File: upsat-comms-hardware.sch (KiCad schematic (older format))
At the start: 195 parts, among them J1 SMA, J2 SMA, P1 SWD, P2 OBC, P3 CONN_02X03, U1 TXCO_TG_5021CG, U10 CC1120, U12 ADT7420, U14 OPA320, U16 RF5110G, U18 FA_128_, U2 TPS79930, U3 FA_128_, U4 CC1120, U5 STM32F407VG, U6 TXCO_TG_5021CG, U8 TPS79930, Y1 Crystal, Y2 Crystal

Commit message: Cleanup of zones and vias.
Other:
- note added: "TX"
- note removed: "CHECK DISCO GERBER"
- note removed: "EDW ISWS LATHOS \nSTON KOMVO PREPEI\nNA NAI APO PANW?"
- note removed: "MPORW NA THN PARALEIPSW THN 0\n"
- note removed: "MY OBC RX IS THE ACTUALL OBC TX"
- note removed: "Na dw ti ginetai me ta ground klp"
- note removed: "Na dw ti ginetai me ta ground klp kai toy stm gia ton DAC"
- note removed: "TX1"
- note removed: "WILL I PUT THE 0 OHM RES?\n"
- note removed: "distributed connections between RF and digital ground\nTODO check analog ground"
- moved on the sheet: RFSHIELD1
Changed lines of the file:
@@
 LIBS:F4
 LIBS:F4-cache
-LIBS:ADT7420
-LIBS:cc1120
-LIBS:dart-4460
-LIBS:hrs-dm3
-LIBS:tc74
 LIBS:sma
 LIBS:rf5110g
-LIBS:FA-128 32.0000MF20X-K3
-LIBS:fa128
 LIBS:txco_tg_5021cg
 LIBS:opa320
 LIBS:PE4259
 LIBS:TPS79930
-LIBS:FA_128
-LIBS:fa_128_
+LIBS:hrs-dm3
 LIBS:FA_128_
-LIBS:comms-hardware-diploma-theodoridis-cache
 EELAYER 25 0
 EELAYER END
@@
 	1    0    0    -1
 $EndComp
-Text Notes 2100 22750 0    60   ~ 0
-distributed connections between RF and digital ground\nTODO check analog ground
-Text Notes 6150 21900 0    197  ~ 0
-Na dw ti ginetai me ta ground klp
-Text Notes 1100 9900 0    197  ~ 0
-Na dw ti ginetai me ta ground klp kai toy stm gia ton DAC
 Text Notes 1600 18350 0    60   ~ 0
 L1 is a Bead to be mounted if the regulator U2 is not mounted,\nCC1120 ref des will default not use regulator\nCC1120/CC1125: do not mount: U2, C12, C41, C53\nTG5021CG is optional: do not mount L1 if regulator is mounted\n
@@
 	1    0    0    -1
 $EndComp
-Text Notes 2900 2200 0    60   ~ 0
-CHECK DISCO GERBER
 $Comp
 L INDUCTOR L11
@@
 Text Label 12100 3600 0    60   ~ 0
 2GPIO3
-Text Notes 19700 22250 0    60   ~ 0
-MY OBC RX IS THE ACTUALL OBC TX
 Text Notes 28500 2250 0    394  ~ 0
-TX1
+TX
 Text Notes 7900 12350 0    394  ~ 0
 RX
@@
 Text Label 2100 7600 2    60   ~ 0
 USART3_RX
-Text Notes 12600 9300 0    60   ~ 0
-WILL I PUT THE 0 OHM RES?\n
-Text Notes 1250 3000 2    60   ~ 0
-WILL I PUT THE 0 OHM RES?\n
 Text Label 20500 2100 2    60   ~ 0
 I2C1_SCL
@@
 Wire Wire Line
 	3050 17300 2500 17300
-Text Notes 26900 3250 0    60   ~ 0
-EDW ISWS LATHOS \nSTON KOMVO PREPEI\nNA NAI APO PANW?
-Text Notes 7450 9300 0    60   ~ 0
-MPORW NA THN PARALEIPSW THN 0\n
-Text Notes 1800 3450 0    60   ~ 0
-MPORW NA THN PARALEIPSW THN 0\n
 $Comp
 L GND #PWR0129
@@
 L TEST_1P RFSHIELD1
 U 1 1 57080FD5
-P 29350 17650
-F 0 "RFSHIELD1" H 29350 17920 50  0000 C CNN
-F 1 "TEST_1P" H 29350 17850 50  0000 C CNN
-F 2 "libs:BMI-S-x06" H 29550 17650 50  0000 C CNN
-F 3 "" H 29550 17650 50  0000 C CNN
-	1    29350 17650
+P 25150 9500
+F 0 "RFSHIELD1" H 25150 9770 50  0000 C CNN
+F 1 "TEST_1P" H 25150 9700 50  0000 C CNN
+F 2 "libs:BMI-S-x06" H 25350 9500 50  0000 C CNN
+F 3 "" H 25350 9500 50  0000 C CNN
+	1    25150 9500
 	1    0    0    -1
 $EndComp
 Wire Wire Line
-	29350 17650 29350 17900
+	25150 9500 25150 9750
 $Comp
 L GND #PWR0145
 U 1 1 5708250E
-P 29350 17900
-F 0 "#PWR0145" H 29350 17650 50  0001 C CNN
-F 1 "GND" H 29350 17750 50  0000 C CNN
-F 2 "" H 29350 17900 50  0000 C CNN
-F 3 "" H 29350 17900 50  0000 C CNN
-	1    29350 17900
+P 25150 9750
+F 0 "#PWR0145" H 25150 9500 50  0001 C CNN
+F 1 "GND" H 25150 9600 50  0000 C CNN
+F 2 "" H 25150 9750 50  0000 C CNN
+F 3 "" H 25150 9750 50  0000 C CNN
+	1    25150 9750
 	1    0    0    -1
 $EndComp

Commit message: Restructuring libraries.
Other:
- moved on the sheet: C21, C23, C27, C61, C7, C89, C96

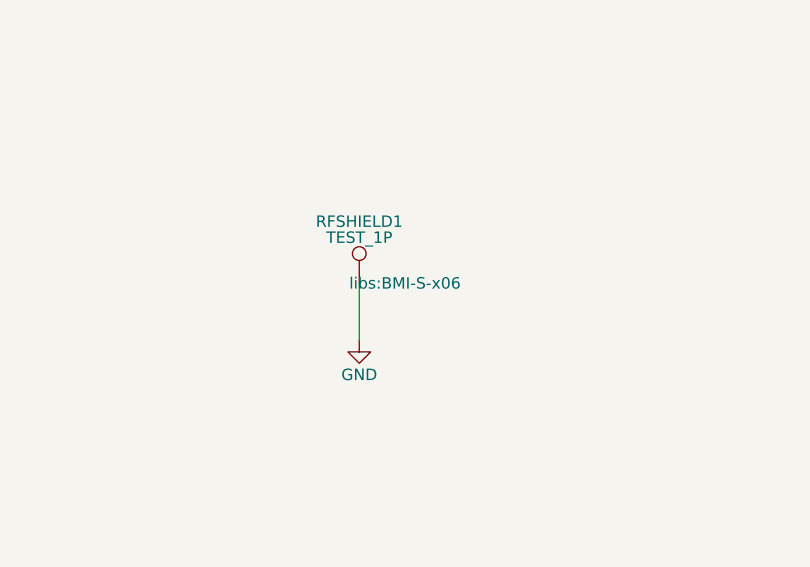
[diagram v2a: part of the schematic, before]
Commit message: Create silkscreen and reroute OBC Connector.
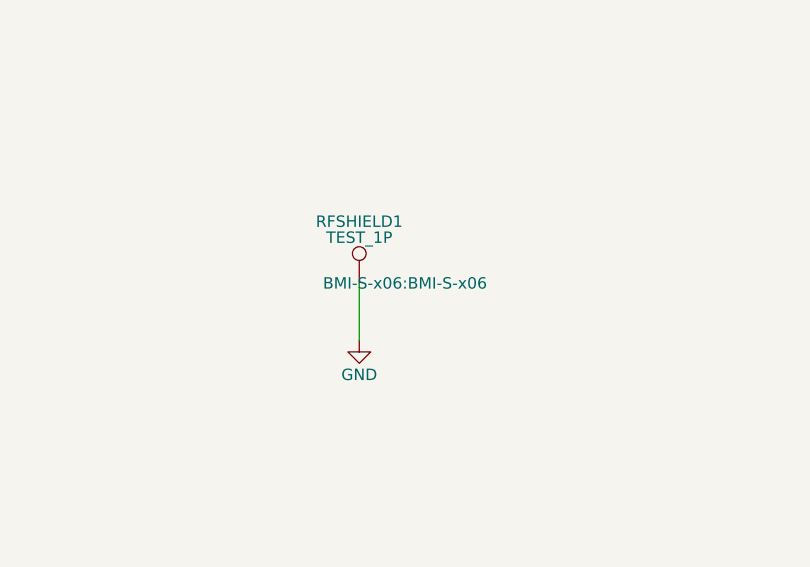
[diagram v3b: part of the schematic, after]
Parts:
- RFSHIELD1: footprint libs:BMI-S-x06 -> BMI-S-x06:BMI-S-x06
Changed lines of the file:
@@
 F 0 "RFSHIELD1" H 25150 9770 50  0000 C CNN
 F 1 "TEST_1P" H 25150 9700 50  0000 C CNN
-F 2 "libs:BMI-S-x06" H 25350 9500 50  0000 C CNN
+F 2 "BMI-S-x06:BMI-S-x06" H 25350 9500 50  0000 C CNN
 F 3 "" H 25350 9500 50  0000 C CNN
 	1    25150 9500

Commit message: Cleanup schematic.
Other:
- note added: "CON"
- note added: "MCU"
- moved on the sheet: C1, C101, C103, C105, C107, C109, C111, C113, C115, C117, C118, C121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

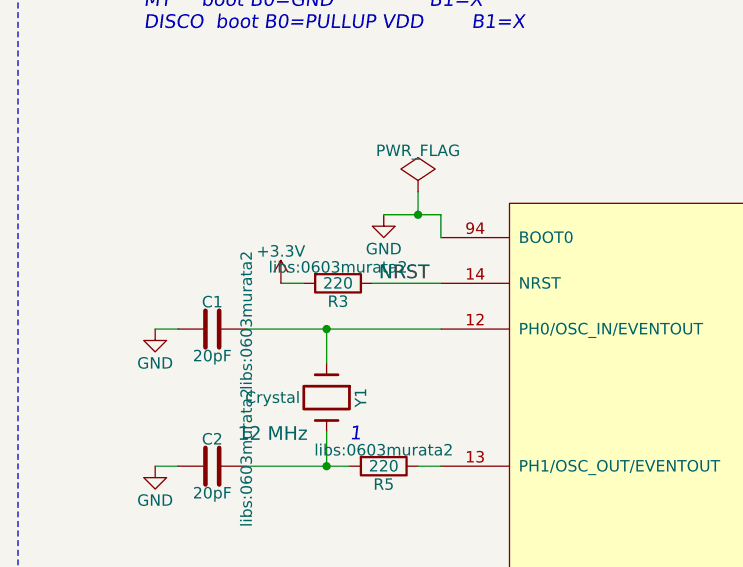
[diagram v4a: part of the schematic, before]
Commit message: Add vias on PA.
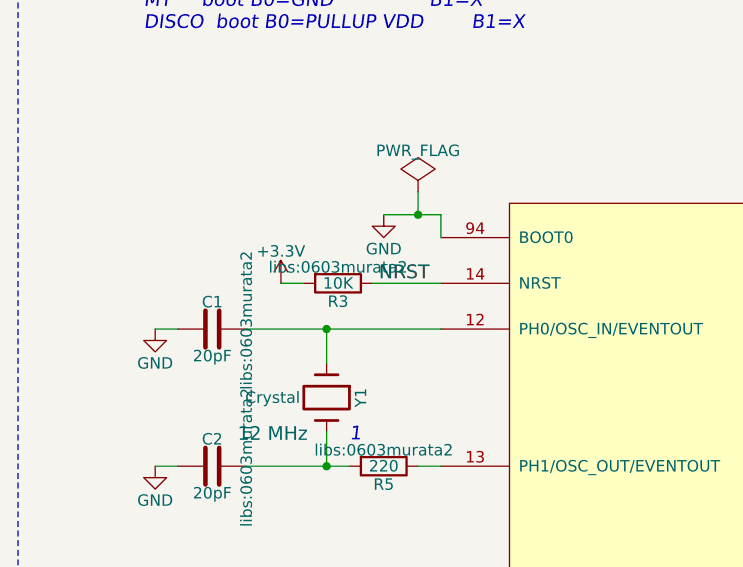
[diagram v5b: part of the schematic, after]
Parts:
- R3: value 220 -> 10K
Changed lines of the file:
@@
 P 2300 3950
 F 0 "R3" V 2380 3950 50  0000 C CNN
-F 1 "220" V 2300 3950 50  0000 C CNN
+F 1 "10K" V 2300 3950 50  0000 C CNN
 F 2 "libs:0603murata2" V 2230 3950 50  0000 C CNN
 F 3 "" H 2300 3950 50  0000 C CNN

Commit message: Routing changes and package fixes.
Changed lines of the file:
@@
 L GND #PWR0147
 U 1 1 5707121B
-P 18450 4350
-F 0 "#PWR0147" H 18450 4100 50  0001 C CNN
-F 1 "GND" H 18450 4200 50  0000 C CNN
-F 2 "" H 18450 4350 50  0000 C CNN
-F 3 "" H 18450 4350 50  0000 C CNN
-	1    18450 4350
+P 18800 4150
+F 0 "#PWR0147" H 18800 3900 50  0001 C CNN
+F 1 "GND" H 18800 4000 50  0000 C CNN
+F 2 "" H 18800 4150 50  0000 C CNN
+F 3 "" H 18800 4150 50  0000 C CNN
+	1    18800 4150
 	-1   0    0    1
 $EndComp
@@
 	3150 14100 3150 13700
 Wire Wire Line
-	3150 13700 2850 13700
-Wire Wire Line
-	2850 13700 2850 12900
+	2850 13700 3150 13700
+Wire Wire Line
+	2850 12900 2850 13700
 Wire Wire Line
 	2850 13100 2950 13100
@@
 	18150 13050 18150 12900
 Wire Wire Line
-	17050 14000 18150 14000
+	18150 14000 17050 14000
 Wire Wire Line
 	17150 14100 18850 14100
@@
 	26100 15450 26100 15400
 Wire Wire Line
-	26100 15400 27350 15400
-Wire Wire Line
-	27350 15400 27350 13750
+	27350 15400 26100 15400
+Wire Wire Line
+	27350 13750 27350 15400
 Wire Wire Line
 	26000 15450 26000 15300
 Wire Wire Line
-	26000 15300 26600 15300
-Wire Wire Line
-	26600 15300 26600 14450
-Wire Wire Line
-	26600 14450 25900 14450
+	26600 15300 26000 15300
+Wire Wire Line
+	26600 14450 26600 15300
+Wire Wire Line
+	25900 14450 26600 14450
 Connection ~ 25900 14850
 Connection ~ 26600 14850
@@
 	15900 14000 15900 13600
 Wire Wire Line
-	15900 13600 15600 13600
-Wire Wire Line
-	15600 13600 15600 12800
+	15600 13600 15900 13600
+Wire Wire Line
+	15600 12800 15600 13600
 Wire Wire Line
 	15600 13000 15700 13000
@@
 	22600 19050 22600 19300
 Wire Wire Line
-	18500 4450 18500 4400
+	18800 4150 18800 4450
 Wire Wire Line
 	18550 2750 18550 2900
@@
 	6000 2250 6000 2300
 Wire Wire Line
-	18500 4450 18850 4450
+	18800 4450 18850 4450
 Wire Wire Line
 	2650 3550 2650 3650
 Connection ~ 2650 3650
 Wire Wire Line
-	18500 4400 18450 4400
-Wire Wire Line
-	18450 4400 18450 4350
-Wire Wire Line
 	25300 15150 25300 16050
 Connection ~ 25300 15700
@@
 Connection ~ 15200 15400
 Wire Wire Line
-	18150 14000 18150 13350
+	18150 13350 18150 14000
 Connection ~ 18150 13650
 Wire Wire Line

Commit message: Fix silkscreen specs.
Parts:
- C17: footprint libs:0603murata2 -> libs:CC1120DecCAP
- U18, U3: footprint w_crystal:crystal_fa128 -> libs:crystal_fa128
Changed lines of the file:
@@
 F 0 "C17" H 4468 19500 50  0000 C CNN
 F 1 "2.2uF" H 4429 19300 50  0000 L CNN
-F 2 "libs:0603murata2" H 4500 19200 50  0000 C CNN
+F 2 "libs:CC1120DecCAP" H 4500 19200 50  0000 C CNN
 F 3 "" H 4350 19400 50  0000 C CNN
 F 4 "0603" H 4350 19400 60  0001 C CNN "PKG"
@@
 F 0 "U18" H 15950 13050 60  0000 C CNN
 F 1 "FA_128_" H 15950 12800 39  0000 C CNN
-F 2 "w_crystal:crystal_fa128" H 15950 13050 60  0000 C CNN
+F 2 "libs:crystal_fa128" H 15950 13050 60  0000 C CNN
 F 3 "" H 15950 13050 60  0000 C CNN
 	1    15950 13050
@@
 F 0 "U3" H 3200 13150 60  0000 C CNN
 F 1 "FA_128_" H 3200 12950 39  0000 C CNN
-F 2 "w_crystal:crystal_fa128" H 3200 13150 60  0000 C CNN
+F 2 "libs:crystal_fa128" H 3200 13150 60  0000 C CNN
 F 3 "" H 3200 13150 60  0000 C CNN
 	1    3200 13150
@@
 	3150 14100 3150 13700
 Wire Wire Line
-	2850 13700 3150 13700
+	3150 13700 2850 13700
 Wire Wire Line
-	2850 12900 2850 13700
+	2850 13700 2850 12900
 Wire Wire Line
 	2850 13100 2950 13100
@@
 	18150 13050 18150 12900
 Wire Wire Line
-	18150 14000 17050 14000
+	17050 14000 18150 14000
 Wire Wire Line
 	17150 14100 18850 14100
@@
 	26100 15450 26100 15400
 Wire Wire Line
-	27350 15400 26100 15400
+	26100 15400 27350 15400
 Wire Wire Line
-	27350 13750 27350 15400
+	27350 15400 27350 13750
 Wire Wire Line
 	26000 15450 26000 15300
 Wire Wire Line
-	26600 15300 26000 15300
+	26000 15300 26600 15300
 Wire Wire Line
-	26600 14450 26600 15300
+	26600 15300 26600 14450
 Wire Wire Line
-	25900 14450 26600 14450
+	26600 14450 25900 14450
 Connection ~ 25900 14850
 Connection ~ 26600 14850
@@
 	15900 14000 15900 13600
 Wire Wire Line
-	15600 13600 15900 13600
+	15900 13600 15600 13600
 Wire Wire Line
-	15600 12800 15600 13600
+	15600 13600 15600 12800
 Wire Wire Line
 	15600 13000 15700 13000
@@
 Connection ~ 15200 15400
 Wire Wire Line
-	18150 13350 18150 14000
+	18150 14000 18150 13350
 Connection ~ 18150 13650
 Wire Wire Line

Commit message: Exchange SOT23-5 footprint.
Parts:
- U14, U2, U8: footprint libs:SOT23-5 -> w_smd_trans:sot23-5
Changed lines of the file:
@@
 U 1 1 56FC6AC1
 P 3000 19250
-F 0 "U2" H 3000 19250 60  0000 C CNN
+F 0 "U2" H 3000 19350 60  0000 C CNN
 F 1 "TPS79930" H 3000 19600 60  0000 C CNN
-F 2 "libs:SOT23-5" H 3000 19250 60  0000 C CNN
+F 2 "w_smd_trans:sot23-5" H 3000 19250 60  0000 C CNN
 F 3 "" H 3000 19250 60  0000 C CNN
 	1    3000 19250
@@
 F 0 "U14" H 25000 13350 50  0000 C CNN
 F 1 "OPA320" H 25100 13000 50  0000 C CNN
-F 2 "libs:SOT23-5" H 24850 12900 50  0000 L CNN
+F 2 "w_smd_trans:sot23-5" H 24850 12900 50  0000 L CNN
 F 3 "" H 24950 13400 50  0000 C CNN
 	1    24900 13200
@@
 F 0 "U8" H 15800 19100 60  0000 C CNN
 F 1 "TPS79930" H 15750 19500 60  0000 C CNN
-F 2 "libs:SOT23-5" H 15800 18800 60  0000 C CNN
+F 2 "w_smd_trans:sot23-5" H 15800 18800 60  0000 C CNN
 F 3 "" H 15750 19150 60  0000 C CNN
 	1    15750 19150
